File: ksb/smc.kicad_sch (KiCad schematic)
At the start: 15 parts, among them U4 X850744-001

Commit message: Internal Connectors
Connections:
- net EXPPORT_RJ45.D+ is gone; now on net EXPPORT_PORT3.D+: U4.J2 (USBA_D3_DP)
- net EXPPORT_RJ45.D- is gone; now on net EXPPORT_PORT3.D-: U4.J1 (USBA_D3_DN)
- net EXPPORT_PORT1.D+: now also U4.K3 (USBA_D1_DP); no longer U4.M3 (USBA_D2_DP)
- net EXPPORT_PORT1.D-: now also U4.K2 (USBA_D1_DN); no longer U4.M2 (USBA_D2_DN)
- net EXPPORT_PORT2.D+: now also U4.M3 (USBA_D2_DP); no longer U4.L2 (USBA_D0_DP)
- net EXPPORT_PORT2.D-: now also U4.M2 (USBA_D2_DN); no longer U4.L1 (USBA_D0_DN)
- net EXPPORT_PORT3.D+: no longer U4.K3 (USBA_D1_DP)
- net EXPPORT_PORT3.D-: no longer U4.K2 (USBA_D1_DN)
- new net EXPPORT_PORT0.D+: U4.L2 (USBA_D0_DP)
- new net EXPPORT_PORT0.D-: U4.L1 (USBA_D0_DN)
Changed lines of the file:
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@@
 	(bus
 		(pts
-			(xy 40.64 143.51) (xy 45.72 143.51)
+			(xy 43.18 143.51) (xy 45.72 143.51)
 		)
 		(stroke
@@
 	(bus
 		(pts
-			(xy 152.4 60.96) (xy 147.32 60.96)
-		)
-		(stroke
-			(width 0)
-			(type default)
-		)
-	)
-	(bus
-		(pts
-			(xy 143.51 133.35) (xy 138.43 133.35)
-		)
-		(stroke
-			(width 0)
-			(type default)
-		)
-	)
-	(bus
-		(pts
-			(xy 152.4 68.58) (xy 147.32 68.58)
+			(xy 152.4 60.96) (xy 149.86 60.96)
+		)
+		(stroke
+			(width 0)
+			(type default)
+		)
+	)
+	(bus
+		(pts
+			(xy 140.97 133.35) (xy 138.43 133.35)
+		)
+		(stroke
+			(width 0)
+			(type default)
+		)
+	)
+	(bus
+		(pts
+			(xy 152.4 68.58) (xy 149.86 68.58)
 		)
 		(stroke
@@
 	(bus
 		(pts
-			(xy 143.51 156.21) (xy 138.43 156.21)
+			(xy 140.97 156.21) (xy 138.43 156.21)
 		)
 		(stroke
@@
 	(bus
 		(pts
-			(xy 265.43 30.48) (xy 270.51 30.48)
+			(xy 265.43 30.48) (xy 265.43 27.94)
 		)
 		(stroke
@@
 	(bus
 		(pts
-			(xy 152.4 76.2) (xy 147.32 76.2)
+			(xy 152.4 76.2) (xy 149.86 76.2)
 		)
 		(stroke
@@
 	(bus
 		(pts
-			(xy 151.13 92.71) (xy 146.05 92.71)
+			(xy 148.59 92.71) (xy 146.05 92.71)
 		)
 		(stroke
@@
 	(bus
 		(pts
-			(xy 250.19 58.42) (xy 255.27 58.42)
+			(xy 250.19 58.42) (xy 252.73 58.42)
 		)
 		(stroke
@@
 	(bus
 		(pts
-			(xy 45.72 100.33) (xy 50.8 100.33)
+			(xy 48.26 100.33) (xy 50.8 100.33)
 		)
 		(stroke
@@
 	(bus
 		(pts
-			(xy 250.19 50.8) (xy 255.27 50.8)
+			(xy 250.19 50.8) (xy 252.73 50.8)
 		)
 		(stroke
@@
 	(bus
 		(pts
-			(xy 255.27 81.28) (xy 260.35 81.28)
+			(xy 255.27 81.28) (xy 257.81 81.28)
 		)
 		(stroke
@@
 	(bus
 		(pts
-			(xy 265.43 91.44) (xy 260.35 91.44)
+			(xy 262.89 91.44) (xy 260.35 91.44)
 		)
 		(stroke
@@
 	(bus
 		(pts
-			(xy 152.4 83.82) (xy 147.32 83.82)
+			(xy 152.4 83.82) (xy 149.86 83.82)
 		)
 		(stroke
@@
 	(bus
 		(pts
-			(xy 250.19 66.04) (xy 255.27 66.04)
+			(xy 250.19 66.04) (xy 252.73 66.04)
 		)
 		(stroke
@@
 	(bus
 		(pts
-			(xy 137.16 30.48) (xy 142.24 30.48)
+			(xy 142.24 27.94) (xy 142.24 30.48)
 		)
 		(stroke
@@
 	(bus
 		(pts
-			(xy 143.51 110.49) (xy 138.43 110.49)
+			(xy 140.97 110.49) (xy 138.43 110.49)
 		)
 		(stroke
@@
 	(bus
 		(pts
-			(xy 40.64 120.65) (xy 45.72 120.65)
+			(xy 43.18 120.65) (xy 45.72 120.65)
 		)
 		(stroke
@@
 		)
 	)
-	(label "EXPPORT_PORT3.D+"
+	(label "EXPPORT_PORT1.D+"
 		(at 175.26 78.74 180)
 		(effects
@@
 		)
 	)
-	(label "EXPPORT_PORT2.D-"
+	(label "EXPPORT_PORT0.D-"
 		(at 175.26 88.9 180)
 		(effects
@@
 		)
 	)
-	(label "EXPPORT_PORT1.D+"
+	(label "EXPPORT_PORT2.D+"
 		(at 175.26 71.12 180)
 		(effects
@@
 		)
 	)
-	(label "EXPPORT_PORT3.D-"
+	(label "EXPPORT_PORT1.D-"
 		(at 175.26 81.28 180)
 		(effects
@@
 		)
 	)
-	(label "EXPPORT_PORT2.D+"
+	(label "EXPPORT_PORT0.D+"
 		(at 175.26 86.36 180)
 		(effects
@@
 		)
 	)
-	(label "EXPPORT_PORT1.D-"
+	(label "EXPPORT_PORT2.D-"
 		(at 175.26 73.66 180)
 		(effects
@@
 		)
 	)
-	(label "EXPPORT_RJ45.D-"
+	(label "EXPPORT_PORT3.D-"
 		(at 175.26 66.04 180)
 		(effects
@@
 		)
 	)
-	(label "EXPPORT_RJ45.D+"
+	(label "EXPPORT_PORT3.D+"
 		(at 175.26 63.5 180)
 		(effects
@@
 	(hierarchical_label "GAMEPORT2{USB}"
 		(shape bidirectional)
-		(at 255.27 50.8 0)
+		(at 252.73 50.8 0)
 		(effects
 			(font
@@
 		)
 	)
+	(hierarchical_label "EXPPORT_PORT2{USB}"
+		(shape bidirectional)
+		(at 149.86 68.58 180)
+		(effects
+			(font
+				(size 1.27 1.27)
+			)
+			(justify right)
+		)
+	)
+	(hierarchical_label "SMC{P2_GPIO[0..7]}"
+		(shape bidirectional)
+		(at 140.97 110.49 0)
+		(effects
+			(font
+				(size 1.27 1.27)
+			)
+			(justify left)
+		)
+	)
+	(hierarchical_label "EXPPORT_PORT0{USB}"
+		(shape bidirectional)
+		(at 149.86 83.82 180)
+		(effects
+			(font
+				(size 1.27 1.27)
+			)
+			(justify right)
+		)
+	)
 	(hierarchical_label "EXPPORT_PORT1{USB}"
 		(shape bidirectional)
-		(at 147.32 68.58 180)
-		(effects
-			(font
-				(size 1.27 1.27)
-			)
-			(justify right)
-		)
-	)
-	(hierarchical_label "SMC{P2_GPIO[0..7]}"
-		(shape bidirectional)
-		(at 143.51 110.49 0)
-		(effects
-			(font
-				(size 1.27 1.27)
-			)
-			(justify left)
-		)
-	)
-	(hierarchical_label "EXPPORT_PORT2{USB}"
-		(shape bidirectional)
-		(at 147.32 83.82 180)
-		(effects
-			(font
-				(size 1.27 1.27)
-			)
-			(justify right)
-		)
-	)
-	(hierarchical_label "EXPPORT_PORT3{USB}"
-		(shape bidirectional)
-		(at 147.32 76.2 180)
+		(at 149.86 76.2 180)
 		(effects
 			(font
@@
 	(hierarchical_label "{FLASH}"
 		(shape bidirectional)
-		(at 137.16 30.48 180)
-		(effects
-			(font
-				(size 1.27 1.27)
-			)
-			(justify right)
+		(at 142.24 27.94 90)
+		(effects
+			(font
+				(size 1.27 1.27)
+			)
+			(justify left)
 		)
 	)
 	(hierarchical_label "SMC{P3_GPIO[0..7]}"
 		(shape bidirectional)
-		(at 40.64 143.51 180)
+		(at 43.18 143.51 180)
 		(effects
 			(font
@@
 	(hierarchical_label "{FLASH}"
 		(shape bidirectional)
-		(at 270.51 30.48 0)
+		(at 265.43 27.94 90)
 		(effects
 			(font
@@
 	(hierarchical_label "BORONFPMPORT{USB}"
 		(shape bidirectional)
-		(at 260.35 81.28 0)
+		(at 257.81 81.28 0)
 		(effects
 			(font
@@
 	(hierarchical_label "WAVEPORT{USB}"
 		(shape bidirectional)
-		(at 255.27 58.42 0)
+		(at 252.73 58.42 0)
 		(effects
 			(font
@@
 	(hierarchical_label "SMC{UART}"
 		(shape bidirectional)
-		(at 45.72 100.33 180)
+		(at 48.26 100.33 180)
 		(effects
 			(font
@@
 	(hierarchical_label "KSB{SPI}"
 		(shape bidirectional)
-		(at 265.43 91.44 0)
+		(at 262.89 91.44 0)
 		(effects
 			(font
@@
 	(hierarchical_label "SMC{P0_GPIO[0..7]}"
 		(shape bidirectional)
-		(at 143.51 156.21 0)
+		(at 140.97 156.21 0)
 		(effects
 			(font
@@
 	(hierarchical_label "SMC{UART}"
 		(shape bidirectional)
-		(at 151.13 92.71 0)
+		(at 148.59 92.71 0)
 		(effects
 			(font
@@
 	(hierarchical_label "SMC{P1_GPIO[0..7]}"
 		(shape bidirectional)
-		(at 143.51 133.35 0)
+		(at 140.97 133.35 0)
 		(effects
 			(font
@@
 	(hierarchical_label "GAMEPORT1{USB}"
 		(shape bidirectional)
-		(at 255.27 66.04 0)
+		(at 252.73 66.04 0)
 		(effects
 			(font
@@
 	(hierarchical_label "SMC{P4_GPIO[0..7]}"
 		(shape bidirectional)
-		(at 40.64 120.65 180)
+		(at 43.18 120.65 180)
 		(effects
 			(font
@@
 		)
 	)
-	(hierarchical_label "EXPPORT_PORT4{USB}"
+	(hierarchical_label "EXPPORT_PORT3{USB}"
 		(shape bidirectional)
-		(at 147.32 60.96 180)
-		(effects
-			(font
+		(at 149.86 60.96 180)
+		(effects
+			(font

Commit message: Cleanup & Debug I/O
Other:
- moved on the sheet: C243
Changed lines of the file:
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@@
 	)
 	(junction
-		(at 48.26 78.74)
+		(at 48.26 80.01)
 		(diameter 0)
 		(color 0 0 0 0)
@@
 	(wire
 		(pts
-			(xy 45.72 78.74) (xy 48.26 78.74)
+			(xy 45.72 80.01) (xy 48.26 80.01)
 		)
 		(stroke
@@
 	(wire
 		(pts
-			(xy 58.42 78.74) (xy 48.26 78.74)
+			(xy 58.42 80.01) (xy 48.26 80.01)
 		)
 		(stroke
@@
 	(wire
 		(pts
-			(xy 58.42 95.25) (xy 58.42 78.74)
+			(xy 58.42 95.25) (xy 58.42 80.01)
 		)
 		(stroke
@@
 	(wire
 		(pts
-			(xy 48.26 81.28) (xy 48.26 78.74)
+			(xy 48.26 82.55) (xy 48.26 80.01)
 		)
 		(stroke
@@
 	(hierarchical_label "SMC_RST_N"
 		(shape input)
-		(at 45.72 78.74 180)
+		(at 45.72 80.01 180)
 		(effects
 			(font
@@
 	(symbol
 		(lib_id "Device:C")
-		(at 48.26 85.09 0)
+		(at 48.26 86.36 0)
 		(unit 1)
 		(exclude_from_sim no)
@@
 		(dnp no)
 		(property "Reference" "C243"
-			(at 50.8 83.82 0)
+			(at 50.8 85.09 0)
 			(effects
 				(font
@@
 		)
 		(property "Value" "1u"
-			(at 50.8 86.36 0)
+			(at 50.8 87.63 0)
 			(effects
 				(font
@@
 		)
 		(property "Footprint" ""
-			(at 49.2252 88.9 0)
+			(at 49.2252 90.17 0)
 			(effects
 				(font
@@
 		)
 		(property "Datasheet" "~"
-			(at 48.26 85.09 0)
+			(at 48.26 86.36 0)
 			(effects
 				(font
@@
 		)
 		(property "Description" "Unpolarized capacitor"
-			(at 48.26 85.09 0)
+			(at 48.26 86.36 0)
 			(effects
 				(font
@@
 	(symbol
 		(lib_id "power:GND")
-		(at 48.26 88.9 0)
+		(at 48.26 90.17 0)
 		(unit 1)
 		(exclude_from_sim no)
@@
 		(fields_autoplaced yes)
 		(property "Reference" "#PWR0111"
-			(at 48.26 95.25 0)
+			(at 48.26 96.52 0)
 			(effects
 				(font
@@
 		)
 		(property "Value" "GND"
-			(at 48.26 93.98 0)
+			(at 48.26 95.25 0)
 			(effects
 				(font
@@
 		)
 		(property "Footprint" ""
-			(at 48.26 88.9 0)
+			(at 48.26 90.17 0)
 			(effects
 				(font
@@
 		)
 		(property "Datasheet" ""
-			(at 48.26 88.9 0)
+			(at 48.26 90.17 0)
 			(effects
 				(font
@@
 		)
 		(property "Description" "Power symbol creates a global label with name \"GND\" , ground"
-			(at 48.26 88.9 0)
+			(at 48.26 90.17 0)
 			(effects
 				(font

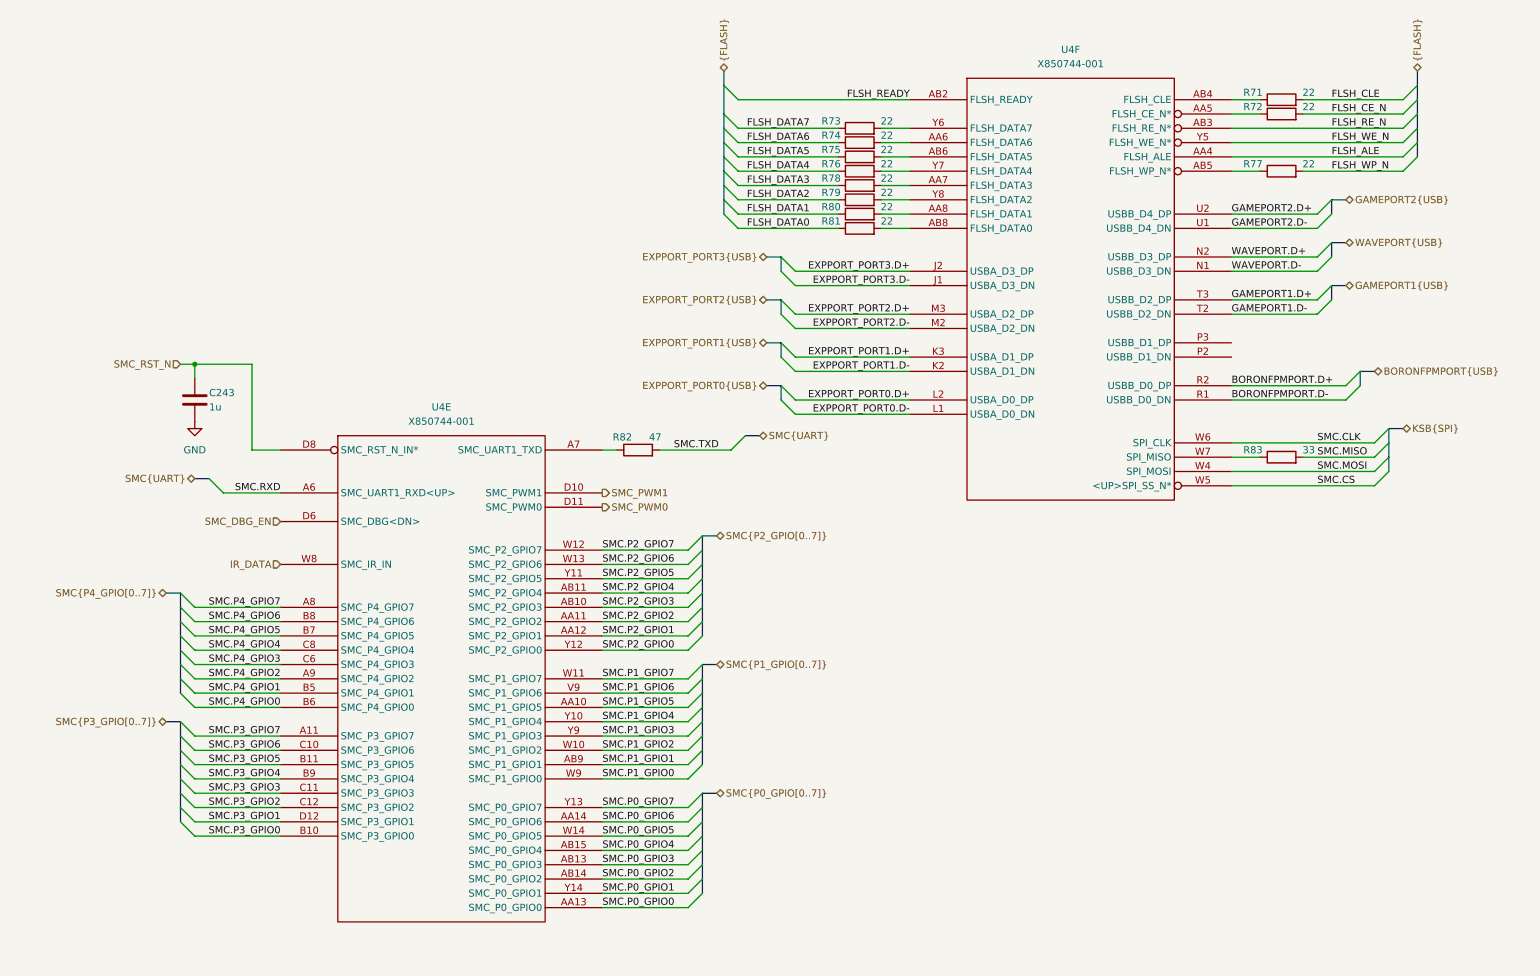
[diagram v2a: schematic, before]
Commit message: Nand Flash, Sata Connectors and removing (hopefully) unnecessary things
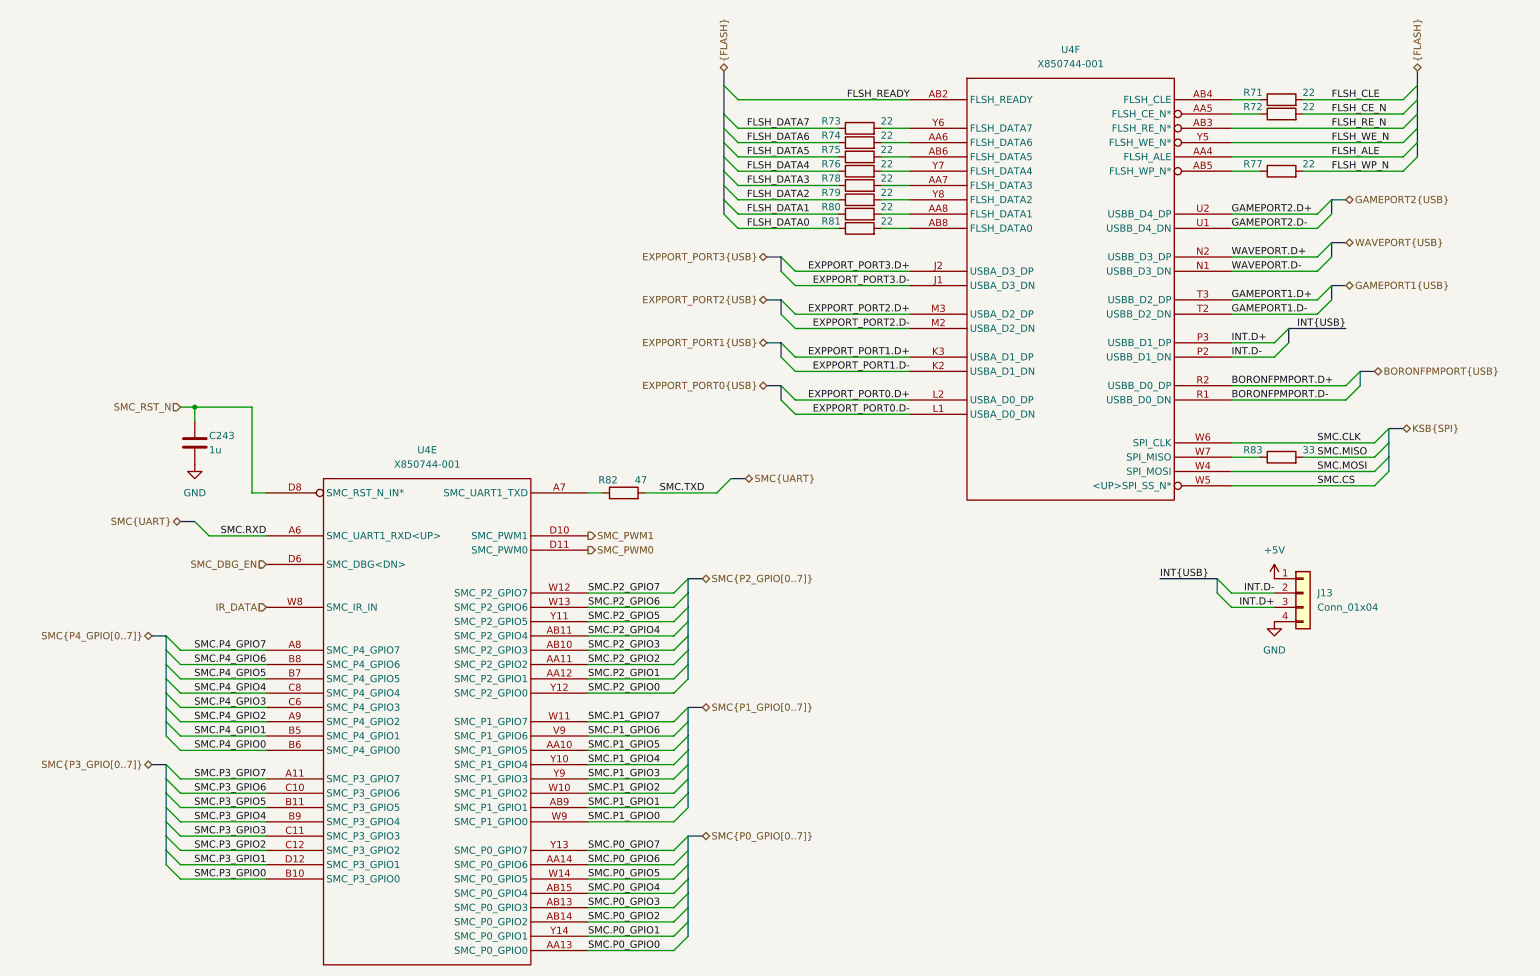
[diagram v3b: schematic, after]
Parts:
- added J13: Conn_01x04, symbol Connector_Generic:Conn_01x04
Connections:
- net GND: now also J13.4 (Pin_4)
- net INT.D-: now reaches U4.P2 (USBB_D1_DN)
- net INT.D-: now also J13.2 (Pin_2)
- net INT.D+: now reaches U4.P3 (USBB_D1_DP)
- net INT.D+: now also J13.3 (Pin_3)
- new net +5V: J13.1 (Pin_1)
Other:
- moved on the sheet: C243, R82, U4E
